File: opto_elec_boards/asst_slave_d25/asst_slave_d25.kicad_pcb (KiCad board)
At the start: 2 copper layers, 91.4 x 91.4 mm, 41 parts, among them J1 FromMainBoard, J3 PID_Int_OK, J4 PID_Der_OK, J5 CLOSE, M4a MountingHole_4.3mm_M4, M4b MountingHole_4.3mm_M4, M4c MountingHole_4.3mm_M4, M4d MountingHole_4.3mm_M4, U1 TL084, U2 TL084

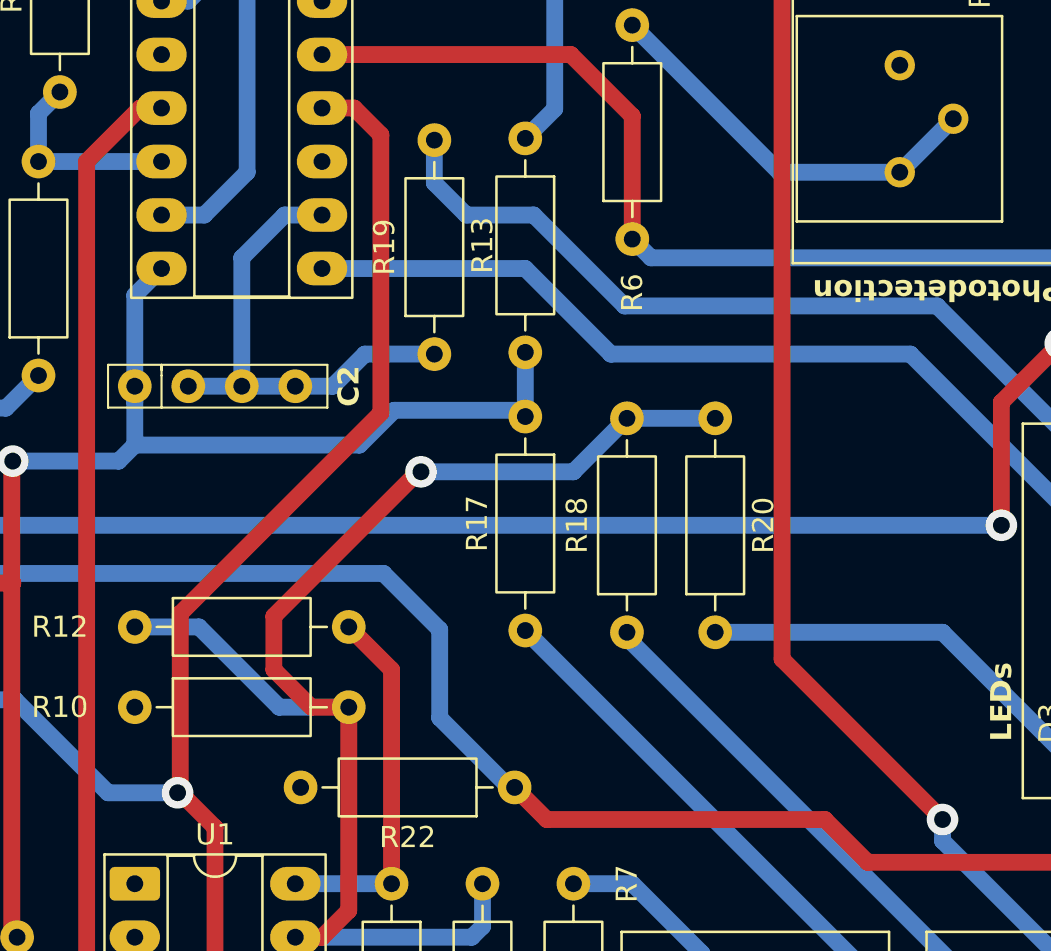
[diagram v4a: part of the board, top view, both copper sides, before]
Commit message: Update OPTO Board / Finish Main -  Photodetec - Control
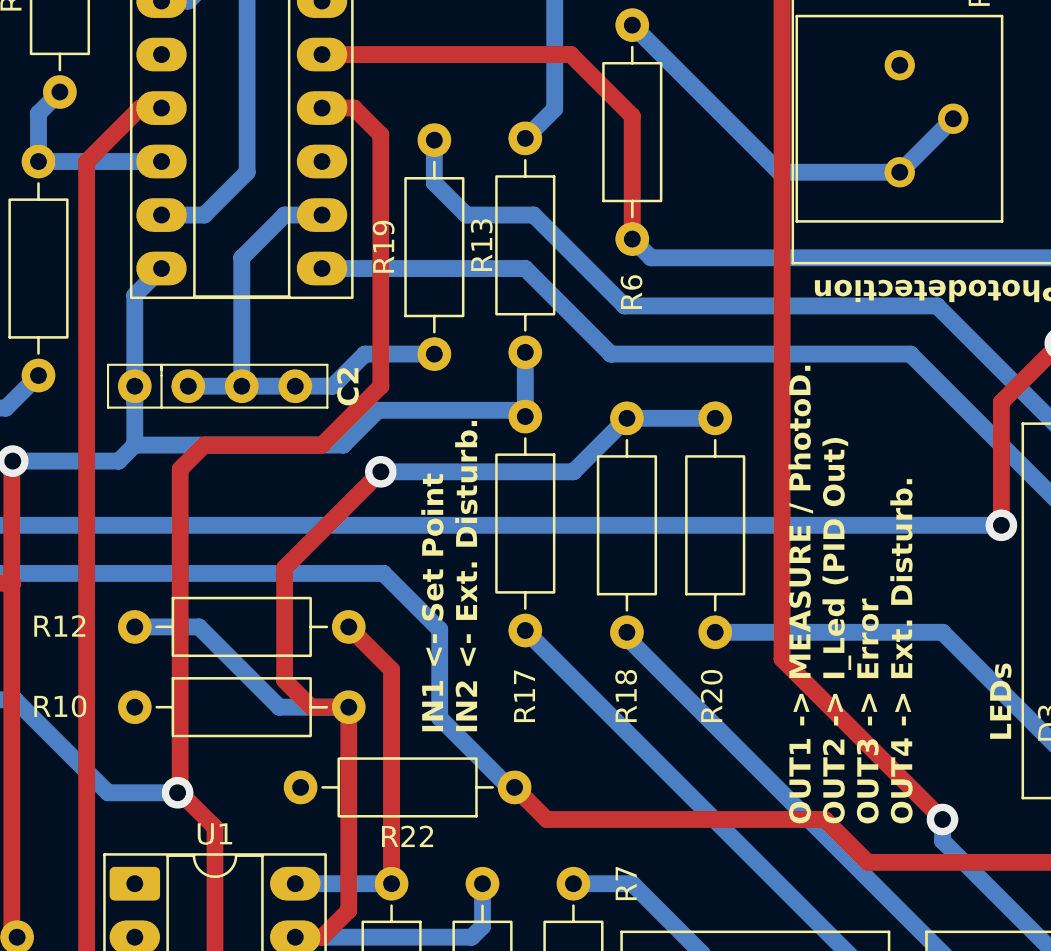
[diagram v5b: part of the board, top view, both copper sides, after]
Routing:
- net -15V: track 73.3 -> 76.6 mm
- net Net-(U1D--): track 67.3 -> 67.9 mm
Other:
- board text added: "IN1 <- Set Point IN2 <- Ext. Disturb."
- board text added: "OUT1 -> MEASURE / PhotoD. OUT2 -> I_Led (PID Out) OUT3 -> Error OUT4 -> Ext. Disturb."
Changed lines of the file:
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@@
 		(tags "Resistor Axial_DIN0207 series Axial Horizontal pin pitch 10.16mm 0.25W = 1/4W length 6.3mm diameter 2.5mm")
 		(property "Reference" "R17"
-			(at 5.08 2.286 90)
+			(at 13.292 0 90)
 			(layer "F.SilkS")
 			(effects
@@
 		(tags "Resistor Axial_DIN0207 series Axial Horizontal pin pitch 10.16mm 0.25W = 1/4W length 6.3mm diameter 2.5mm")
 		(property "Reference" "R20"
-			(at 5.08 2.286 90)
+			(at -3.048 -0.127 90)
 			(layer "F.SilkS")
 			(effects
@@
 		(tags "Resistor Axial_DIN0207 series Axial Horizontal pin pitch 10.16mm 0.25W = 1/4W length 6.3mm diameter 2.5mm")
 		(property "Reference" "R18"
-			(at 5.08 -2.37 90)
+			(at -3.048 0 90)
 			(layer "F.SilkS")
 			(effects
@@
 		)
 	)
+	(gr_text "IN1 <- Set Point\nIN2 <- Ext. Disturb."
+		(at 88.392 85.852 90)
+		(layer "F.SilkS")
+		(effects
+			(font
+				(size 1 1)
+				(thickness 0.2)
+				(bold yes)
+			)
+			(justify left)
+		)
+	)
 	(gr_text "OPTO Illuminance Control"
 		(at 106.426 121.158 180)
@@
 		)
 	)
+	(gr_text "OUT1 -> MEASURE / PhotoD.\nOUT2 -> I_Led (PID Out)\nOUT3 -> Error\nOUT4 -> Ext. Disturb."
+		(at 107.442 90.17 90)
+		(layer "F.SilkS")
+		(effects
+			(font
+				(size 1 1)
+				(thickness 0.2)
+				(bold yes)
+			)
+			(justify left)
+		)
+	)
 	(gr_text "LEDs"
 		(at 114.554 84.328 90)
@@
 	)
 	(segment
-		(start 81.026 100.584)
-		(end 78.486 100.584)
+		(start 85.09 69.342)
+		(end 85.09 57.404)
 		(width 0.8)
 		(layer "F.Cu")
@@
 	)
 	(segment
-		(start 85.09 70.612)
-		(end 85.09 57.404)
+		(start 75.565 73.279)
+		(end 76.708 72.136)
+		(width 0.8)
+		(layer "F.Cu")
+		(net 11)
+	)
+	(segment
+		(start 76.708 72.136)
+		(end 82.296 72.136)
+		(width 0.8)
+		(layer "F.Cu")
+		(net 11)
+	)
+	(segment
+		(start 83.82 56.134)
+		(end 82.296 56.134)
 		(width 0.8)
 		(layer "F.Cu")
@@
 	)
 	(segment
-		(start 77.216 99.314)
-		(end 77.216 90.297)
+		(start 82.296 72.136)
+		(end 85.09 69.342)
 		(width 0.8)
 		(layer "F.Cu")
@@
 	)
 	(segment
-		(start 75.565 80.137)
-		(end 85.09 70.612)
+		(start 78.486 100.584)
+		(end 77.216 99.314)
 		(width 0.8)
 		(layer "F.Cu")
@@
 	)
 	(segment
-		(start 77.216 90.297)
-		(end 75.565 88.646)
+		(start 81.026 100.584)
+		(end 78.486 100.584)
 		(width 0.8)
 		(layer "F.Cu")
@@
 	)
 	(segment
-		(start 83.82 56.134)
-		(end 82.296 56.134)
+		(start 77.216 99.314)
+		(end 77.216 90.297)
 		(width 0.8)
 		(layer "F.Cu")
@@
 	(segment
 		(start 75.565 88.646)
-		(end 75.565 80.137)
+		(end 75.565 73.279)
 		(width 0.8)
 		(layer "F.Cu")
@@
 	)
 	(segment
-		(start 78.486 100.584)
-		(end 77.216 99.314)
+		(start 77.216 90.297)
+		(end 75.565 88.646)
 		(width 0.8)
 		(layer "F.Cu")
@@
 	)
 	(segment
-		(start 91.651 70.485)
-		(end 91.948 70.782)
-		(width 0.8)
-		(layer "B.Cu")
-		(net 18)
-	)
-	(segment
 		(start 73.406 65.024)
 		(end 74.676 63.754)
@@
 	)
 	(segment
-		(start 85.725 70.485)
+		(start 84.963 70.485)
 		(end 91.651 70.485)
 		(width 0.8)
@@
 	(segment
 		(start 73.406 72.136)
-		(end 84.074 72.136)
+		(end 83.312 72.136)
 		(width 0.8)
 		(layer "B.Cu")
@@
 	)
 	(segment
-		(start 84.074 72.136)
-		(end 85.725 70.485)
+		(start 91.948 67.734)
+		(end 91.948 70.782)
 		(width 0.8)
 		(layer "B.Cu")
@@
 	)
 	(segment
-		(start 91.948 67.734)
+		(start 83.312 72.136)
+		(end 84.963 70.485)
+		(width 0.8)
+		(layer "B.Cu")
+		(net 18)
+	)
+	(segment
+		(start 91.651 70.485)
 		(end 91.948 70.782)
 		(width 0.8)
@@
 	)
 	(segment
-		(start 80.01 82.804)
+		(start 80.518 83.312)
 		(end 81.788 84.582)
 		(width 0.8)
@@
 	)
 	(segment
-		(start 86.995 73.406)
-		(end 86.868 73.406)
-		(width 0.8)
-		(layer "F.Cu")
-		(net 32)
-	)
-	(segment
 		(start 83.566 94.234)
 		(end 82.296 95.504)
@@
 	)
 	(segment
-		(start 86.868 73.406)
-		(end 80.01 80.264)
+		(start 81.788 84.582)
+		(end 83.566 84.582)
 		(width 0.8)
 		(layer "F.Cu")
@@
 	)
 	(segment
-		(start 80.01 80.264)
-		(end 80.01 82.804)
+		(start 80.518 77.978)
+		(end 80.518 83.312)
 		(width 0.8)
 		(layer "F.Cu")
@@
 	)
 	(segment
-		(start 81.788 84.582)
-		(end 83.566 84.582)
+		(start 85.09 73.406)
+		(end 80.518 77.978)
 		(width 0.8)
 		(layer "F.Cu")
@@
 	)
 	(via
-		(at 86.995 73.406)
+		(at 85.09 73.406)
 		(size 1.5)
 		(drill 0.8)
@@
 	)
 	(segment
-		(start 86.995 73.406)
-		(end 94.234 73.406)
+		(start 94.234 73.406)
+		(end 96.774 70.866)
 		(width 0.8)
 		(layer "B.Cu")
@@
 	)
 	(segment
-		(start 94.234 73.406)
-		(end 96.774 70.866)
+		(start 85.09 73.406)
+		(end 94.234 73.406)
 		(width 0.8)
 		(layer "B.Cu")
